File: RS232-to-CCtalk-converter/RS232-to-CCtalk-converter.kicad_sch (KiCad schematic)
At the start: 24 parts, among them J1 DB9_Female, J2 CCtalk Cable, J3 CCtalk Cable, J4 DB9_female_hood, Q1 BC847, Q2 BC856, U1 ST232B, U2 L7805

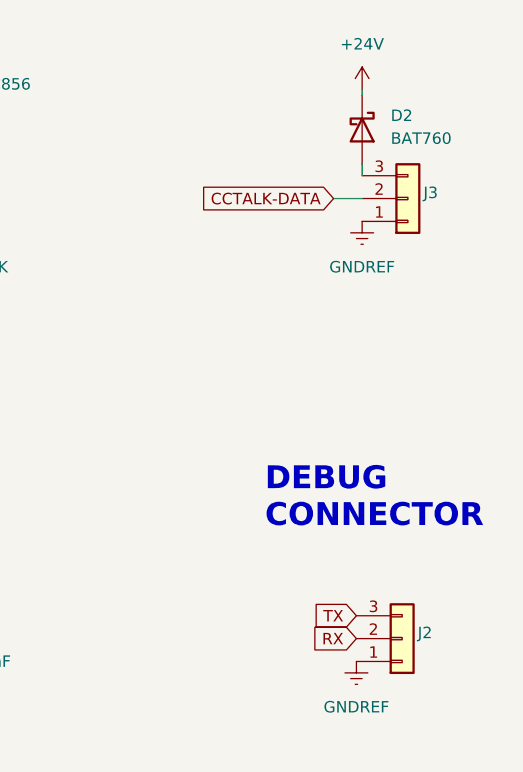
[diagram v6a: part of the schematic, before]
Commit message: implement converter without power supply; its done
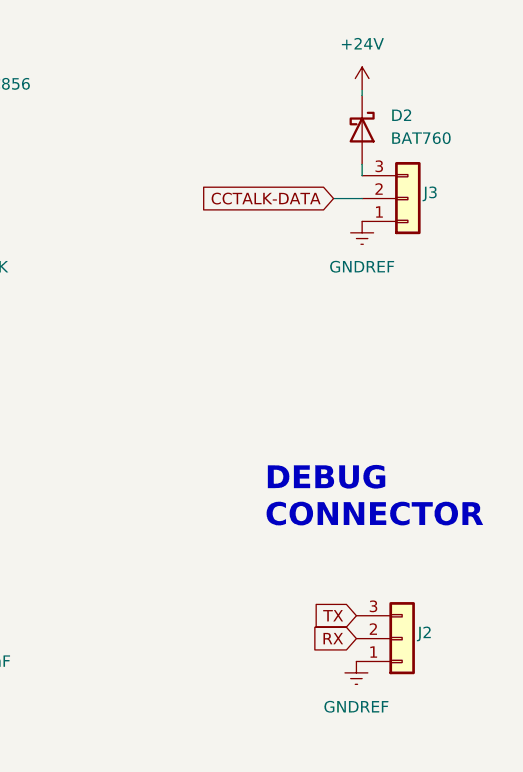
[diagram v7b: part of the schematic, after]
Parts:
- C1, C2, C3, C4, C5, C6, C7, C8, C9: footprint RS232-to-CCtalk-converter-lib:C_0603_1608Metric -> CCtalk-converter-footprints-lib:C_0603_1608Metric; symbol RS232-to-CCtalk-converter-lib:C -> CCtalk-converter-lib:C
- D1, D2: footprint RS232-to-CCtalk-converter-lib:D_SOD-323F -> CCtalk-converter-footprints-lib:D_SOD-323F; symbol RS232-to-CCtalk-converter-lib:BAT54J -> CCtalk-converter-lib:BAT54J
- J2: footprint RS232-to-CCtalk-converter-lib:Header_1x03_P2.54mm_Vertical -> CCtalk-converter-footprints-lib:Header_1x03_P2.54mm_Vertical; symbol RS232-to-CCtalk-converter-lib:Conn_01x03 -> CCtalk-converter-lib:Conn_01x03; MPN (none) -> /
- J3: footprint RS232-to-CCtalk-converter-lib:Header_1x03_P2.54mm_Vertical_with_holder -> CCtalk-converter-footprints-lib:Header_1x03_P2.54mm_Vertical_with_holder; symbol RS232-to-CCtalk-converter-lib:Conn_01x03 -> CCtalk-converter-lib:Conn_01x03; MPN (none) -> /
- J4: footprint RS232-to-CCtalk-converter-lib:DSUB-9_Female_wire_mount_P2.77mm_hood -> CCtalk-converter-footprints-lib:DSUB-9_Female_wire_mount_P2.77mm_hood; symbol RS232-to-CCtalk-converter-lib:DB9_female_hood -> CCtalk-converter-lib:DB9_female_hood
- Q1: footprint RS232-to-CCtalk-converter-lib:SOT-23 -> CCtalk-converter-footprints-lib:SOT-23; symbol RS232-to-CCtalk-converter-lib:BC847 -> CCtalk-converter-lib:BC847
- Q2: footprint RS232-to-CCtalk-converter-lib:SOT-23 -> CCtalk-converter-footprints-lib:SOT-23; symbol RS232-to-CCtalk-converter-lib:BC856 -> CCtalk-converter-lib:BC856
- R1, R2, R3, R4, R5: footprint RS232-to-CCtalk-converter-lib:R_0603_1608Metric -> CCtalk-converter-footprints-lib:R_0603_1608Metric; symbol RS232-to-CCtalk-converter-lib:R -> CCtalk-converter-lib:R
- U1: footprint RS232-to-CCtalk-converter-lib:SOIC-16_4.55x10.3mm_P1.27mm -> CCtalk-converter-lib:SOIC-16_4.55x10.3mm_P1.27mm; symbol RS232-to-CCtalk-converter-lib:ST232B -> CCtalk-converter-lib:ST232B
- U2: footprint RS232-to-CCtalk-converter-lib:TO-252-3_TabPin2 -> CCtalk-converter-footprints-lib:TO-252-3_TabPin2; symbol RS232-to-CCtalk-converter-lib:L7805 -> CCtalk-converter-lib:L7805
